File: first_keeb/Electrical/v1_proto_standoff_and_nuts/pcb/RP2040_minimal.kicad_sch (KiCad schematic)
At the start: 75 parts, among them J1 Conn_01x04_Socket, J2 Conn_01x04_Socket, P1 USB-TYPE-C-016, Q1 SN74LV1T34DBV, SW1 SK-3296S-01-L3, SW2 MS-22C01-G010, SW3 TS-1187A-B-A-B, SW4 MS-22C01-G010, SW5 TS-1187A-B-A-B, SW6 BUTT1, SW7 BUTT3, SW8 BUTT2, U1 AMS1117-2.5, U2 ME6208A44M3G, U3 PRTR5V0U2X, U4 MCP6001-OT, U5 STM32F401RCTx, U6 MCP6001-OT, U7 SLSS49E, U8 SLSS49E, U9 SLSS49E, Y1 8MHz

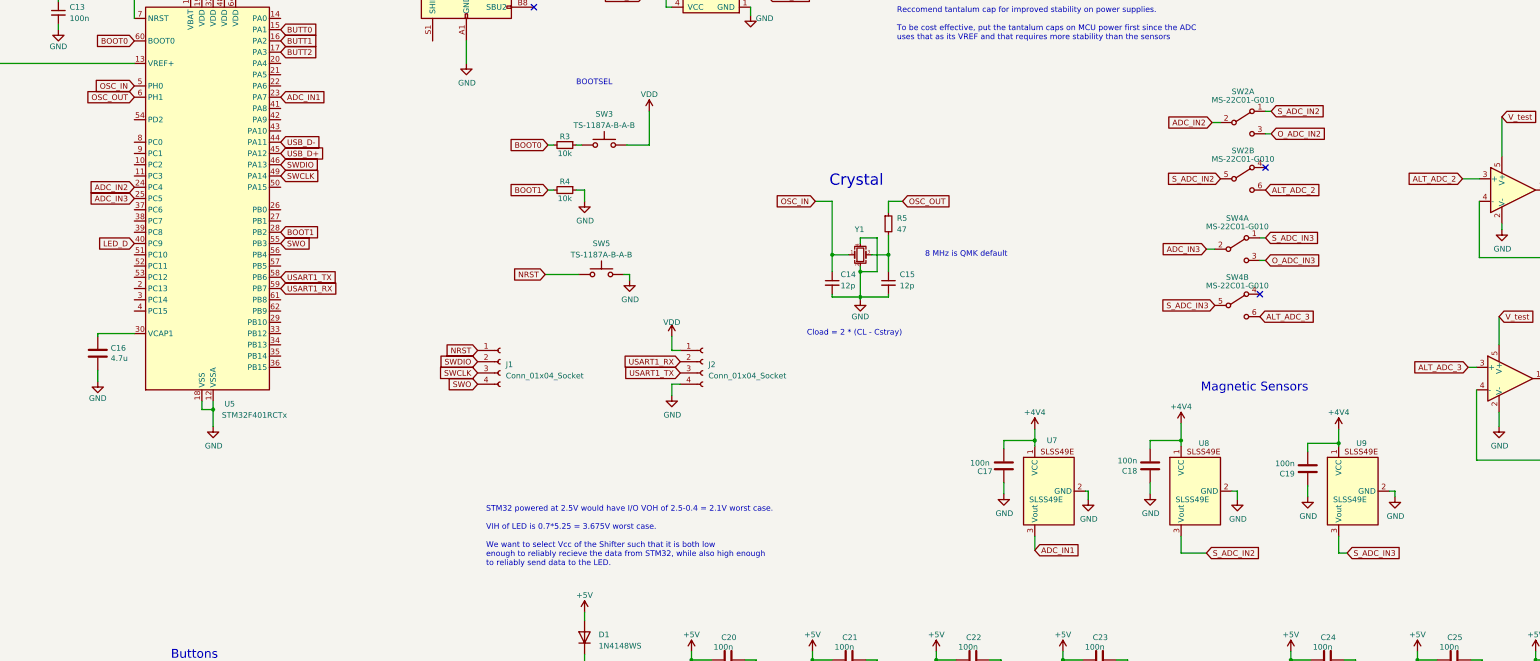
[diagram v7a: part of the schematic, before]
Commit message: creates plate for pcb
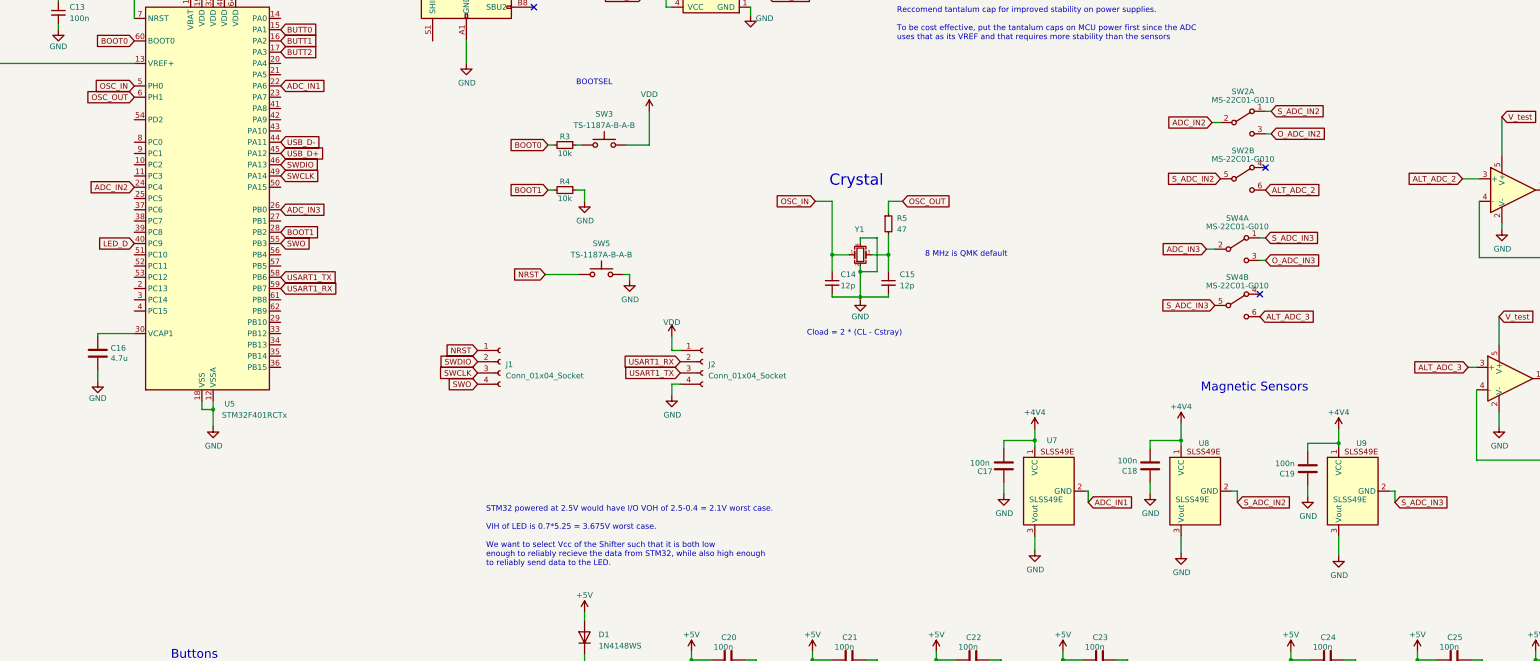
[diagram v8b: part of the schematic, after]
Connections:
- net ADC_IN1: now also U5.22 (PA6), U7.2 (GND); no longer U5.23 (PA7), U7.3 (Vout)
- net ADC_IN3: now also U5.26 (PB0); no longer U5.25 (PC5)
- net GND: now also U7.3 (Vout), U8.3 (Vout), U9.3 (Vout); no longer U7.2 (GND), U8.2 (GND), U9.2 (GND)
- net S_ADC_IN2: now also U8.2 (GND); no longer U8.3 (Vout)
- net S_ADC_IN3: now also U9.2 (GND); no longer U9.3 (Vout)
